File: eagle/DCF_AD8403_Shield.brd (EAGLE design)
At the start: 78.4 x 53.3 mm, 21 parts, among them IC1 TL072P, IC2 AD8403-100, J1 DCIN

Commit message: 基板図仮配線
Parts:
- removed JACK1, JACK2: MJ-353W-0, mylib2:MJ-3052W-0
- removed JP5: TS_SELECT, pinhead:1X03
- added U$1, U$2: AK_RCA_JACK_DIP, mylib2:AK_RCA_JACK_DIP
- moved R3 215.4 mm to (31.8, 33.0), turned to 180 degrees
- moved JP6 206.4 mm to (74.9, 27.9)
- moved C6 190.6 mm to (63.5, 43.2), turned to 90 degrees
- moved C7 187.5 mm to (63.5, 30.5), turned to 90 degrees
- moved C5 178.3 mm to (49.5, 43.2), turned to 180 degrees
- moved R1 161.3 mm to (53.3, 36.8), turned to 90 degrees
- moved R2 161.1 mm to (54.6, 30.5), turned to 180 degrees
- moved C4 160.6 mm to (44.5, 30.5), turned to 180 degrees
- moved C3 141.7 mm to (36.8, 27.9)
- moved C2 129.1 mm to (36.8, 35.6), turned to 180 degrees
- moved C1 128.1 mm to (36.8, 40.6), turned to 180 degrees
- moved J1 10.2 mm to (71.1, 38.1)
- moved IC2 7.62 mm to (29.2, 17.8)
- moved IC1 1.80 mm to (47.0, 36.8), turned to 270 degrees
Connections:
- removed net N$2: JACK1.2, JP5.1
- removed net N$4: JACK1.3, JP5.3
- net AGND: now also U$1.1, U$1.2, U$2.1, U$2.2; no longer JACK1.1, JACK2.1
- net BYPASS: now also U$1.3, U$1.4; no longer JACK2.3
- net FILTERED: now also U$2.3, U$2.4; no longer JACK2.2
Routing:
- net AGND: track 0.00 -> 148.0 mm
- net N$6: track 0.00 -> 87.6 mm
- net VSS: track 0.00 -> 61.1 mm
- net FILTERED: track 0.00 -> 60.1 mm
- net +5V: track 0.00 -> 48.3 mm
- net N$8: track 0.00 -> 47.1 mm
- net VDD: track 0.00 -> 43.6 mm
- net BYPASS: track 0.00 -> 38.7 mm
- net N$1: track 0.00 -> 32.6 mm
- net SCK: track 0.00 -> 25.7 mm
- net GND: track 0.00 -> 23.9 mm
- net N$5: track 0.00 -> 22.9 mm
- net MOSI: track 0.00 -> 10.2 mm
- net CS: track 0.00 -> 5.08 mm

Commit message: Update Eagle Files
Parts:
- removed U$1, U$2: AK_RCA_JACK_DIP, mylib2:AK_RCA_JACK_DIP
- added JK1: AK_RCA_JACK_DIP_REVERSE, mylib2:AK_RCA_JACK_DIP
- added JK2: AK_RCA_JACK_DIP, mylib2:AK_RCA_JACK_DIP
- added LED1: (no value), led:LED3MM
- added R4: 1k, rcl:0204/7
- C4, C5: value (none) -> 0.1uF
- C6, C7: value (none) -> 100uF; device rcl:SANYO-OSCON_E9 -> rcl:E2,5-6
- R1, R2: value (none) -> 100k
- R3: value (none) -> 0
- moved C1 25.4 mm to (36.8, 15.2)
- moved C2 22.7 mm to (26.7, 15.2), turned to 0 degrees
- moved C5 20.9 mm to (69.8, 38.1), turned to 0 degrees
- moved R1 18.5 mm to (71.1, 31.8)
- moved C4 18.5 mm to (62.2, 25.4)
- moved IC1 18.5 mm to (64.8, 31.8)
- moved R2 16.1 mm to (69.8, 25.4), turned to 0 degrees
- moved C7 13.3 mm to (76.2, 26.7), turned to 270 degrees
- moved IC2 11.4 mm to (34.3, 27.9)
- moved C3 10.5 mm to (39.4, 38.1), turned to 180 degrees
- moved R3 9.16 mm to (36.8, 25.4), turned to 0 degrees
- moved JP6 8.98 mm to (76.2, 36.8), turned to 90 degrees
- moved J1 7.62 mm to (71.1, 45.7)
- moved C6 1.27 mm to (62.2, 43.2), turned to 180 degrees
- turned JP1 to 180 degrees
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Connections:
- removed net VDD: C5.1, C6.+, IC1.8, J1.1, JP6.1, R1.2
- removed net VSS: C4.2, C7.-, IC1.4, J1.3, JP6.2, R2.1
- new net N$2: LED1.A, R4.1
- new net V+: C5.1, C6.+, IC1.8, J1.1, JP6.1, R1.2, R4.2
- new net V-: C4.2, C7.-, IC1.4, J1.3, JP6.2, LED1.K, R2.1
- net +5V: now also C3.1; no longer C3.2
- net AGND: now also C3.2, JK1.3, JK1.4, JK2.1, JK2.2, R3.1; no longer R3.2, U$1.1, U$1.2, U$2.1, U$2.2
- net BYPASS: now also JK1.1, JK1.2; no longer U$1.3, U$1.4
- net FILTERED: now also JK2.3, JK2.4; no longer U$2.3, U$2.4
- net GND: now also R3.2; no longer C3.1, R3.1
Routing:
- net N$6: track 87.6 -> 20.3 mm
- net V-: track 0.00 -> 65.1 mm
- net VSS: track 61.1 -> 0.00 mm
- net VDD: track 43.6 -> 0.00 mm
- net FILTERED: track 60.1 -> 85.1 mm
- net V+: track 0.00 -> 23.1 mm
- net N$1: track 32.6 -> 50.4 mm
- net CS: track 5.08 -> 22.0 mm
- net MOSI: track 10.2 -> 22.0 mm
- net SCK: track 25.7 -> 36.8 mm
- net N$8: track 47.1 -> 57.5 mm
- net AGND: track 148.0 -> 138.4 mm
- net GND: track 23.9 -> 33.2 mm
- net +5V: track 48.3 -> 39.2 mm
- net BYPASS: track 38.7 -> 32.6 mm
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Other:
- board size 78.4 x 53.3 mm -> 81 x 53.3 mm

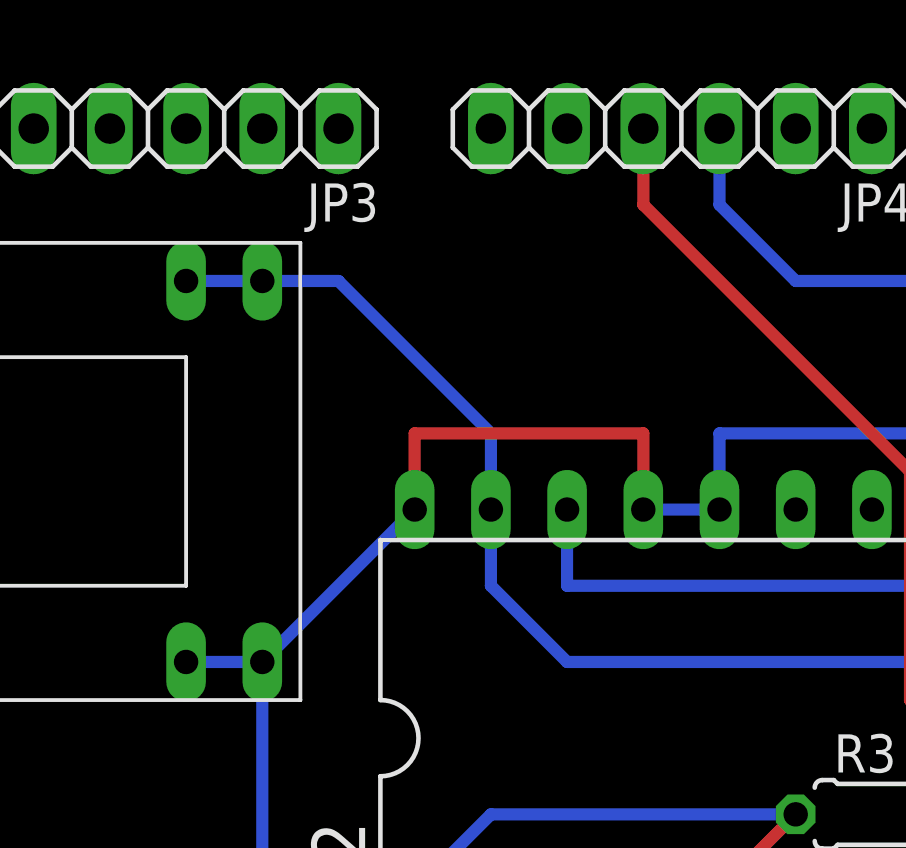
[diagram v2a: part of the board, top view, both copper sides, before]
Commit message: Add: output AC Coupling
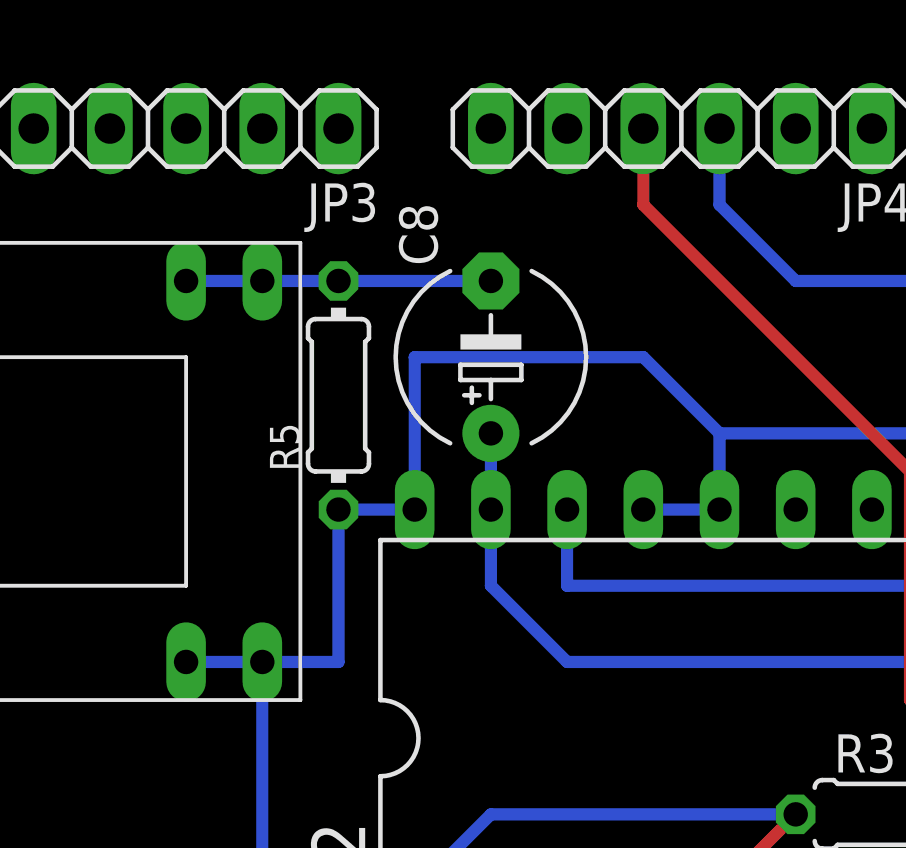
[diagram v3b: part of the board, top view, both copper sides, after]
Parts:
- added C8: 10uF, rcl:E5-6
- added R5: 10k, rcl:0204/7
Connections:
- new net N$3: C8.-, JK2.3, JK2.4, R5.2
- net AGND: now also R5.1
- net FILTERED: now also C8.+; no longer JK2.3, JK2.4
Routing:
- net FILTERED: track 85.1 -> 72.8 mm
- net N$3: track 0.00 -> 10.2 mm
- net AGND: track 138.4 -> 145.0 mm
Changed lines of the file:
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@@
 <element name="LED1" library="led" package="LED3MM" value="" x="60.96" y="49.53" rot="R270"/>
 <element name="R4" library="rcl" package="0204/7" value="1k" x="66.04" y="46.99" rot="R270"/>
+<element name="C8" library="rcl" package="E5-6" value="10uF" x="22.86" y="40.64" rot="R90"/>
+<element name="R5" library="rcl" package="0204/7" value="10k" x="17.78" y="39.37" rot="R90"/>
 </elements>
 <signals>
@@
 <contactref element="IC1" pad="1"/>
 <contactref element="IC2" pad="23"/>
-<contactref element="JK2" pad="3"/>
-<contactref element="JK2" pad="4"/>
-<wire x1="15.24" y1="43.18" x2="12.7" y2="43.18" width="0.4064" layer="16"/>
-<wire x1="15.24" y1="43.18" x2="17.78" y2="43.18" width="0.4064" layer="16"/>
-<wire x1="17.78" y1="43.18" x2="22.86" y2="38.1" width="0.4064" layer="16"/>
-<wire x1="22.86" y1="38.1" x2="22.86" y2="35.56" width="0.4064" layer="16"/>
 <wire x1="22.86" y1="35.56" x2="22.86" y2="33.02" width="0.4064" layer="16"/>
 <wire x1="22.86" y1="33.02" x2="25.4" y2="30.48" width="0.4064" layer="16"/>
@@
 <wire x1="53.34" y1="30.48" x2="58.42" y2="35.56" width="0.4064" layer="16"/>
 <wire x1="58.42" y1="35.56" x2="60.96" y2="35.56" width="0.4064" layer="16"/>
+<contactref element="C8" pad="+"/>
+<wire x1="22.86" y1="38.1" x2="22.86" y2="35.56" width="0.4064" layer="16"/>
 </signal>
 <signal name="N$1">
@@
 <wire x1="12.7" y1="22.86" x2="15.24" y2="22.86" width="0.4064" layer="16"/>
 <wire x1="15.24" y1="30.48" x2="15.24" y2="22.86" width="0.4064" layer="16"/>
-<wire x1="15.24" y1="30.48" x2="20.32" y2="35.56" width="0.4064" layer="16"/>
 <wire x1="15.24" y1="22.86" x2="17.78" y2="20.32" width="0.4064" layer="16"/>
 <wire x1="17.78" y1="20.32" x2="20.32" y2="20.32" width="0.4064" layer="16"/>
@@
 <wire x1="22.86" y1="25.4" x2="33.02" y2="25.4" width="0.4064" layer="16"/>
 <wire x1="27.94" y1="35.56" x2="30.48" y2="35.56" width="0.4064" layer="16"/>
-<wire x1="20.32" y1="35.56" x2="20.32" y2="38.1" width="0.4064" layer="1"/>
-<wire x1="20.32" y1="38.1" x2="27.94" y2="38.1" width="0.4064" layer="1"/>
-<wire x1="27.94" y1="38.1" x2="27.94" y2="35.56" width="0.4064" layer="1"/>
 <wire x1="68.58" y1="33.02" x2="68.58" y2="30.48" width="0.4064" layer="16"/>
 <wire x1="68.58" y1="33.02" x2="66.04" y2="33.02" width="0.4064" layer="16"/>
@@
 <wire x1="38.1" y1="40.64" x2="58.42" y2="40.64" width="0.4064" layer="1"/>
 <wire x1="58.42" y1="40.64" x2="60.96" y2="43.18" width="0.4064" layer="1"/>
+<contactref element="R5" pad="1"/>
+<wire x1="20.32" y1="35.56" x2="20.32" y2="40.64" width="0.4064" layer="16"/>
+<wire x1="20.32" y1="40.64" x2="27.94" y2="40.64" width="0.4064" layer="16"/>
+<wire x1="27.94" y1="40.64" x2="30.48" y2="38.1" width="0.4064" layer="16"/>
+<wire x1="17.78" y1="35.56" x2="20.32" y2="35.56" width="0.4064" layer="16"/>
+<wire x1="17.78" y1="35.56" x2="17.78" y2="30.48" width="0.4064" layer="16"/>
+<wire x1="17.78" y1="30.48" x2="15.24" y2="30.48" width="0.4064" layer="16"/>
+</signal>
+<signal name="N$3">
+<contactref element="C8" pad="-"/>
+<contactref element="JK2" pad="3"/>
+<contactref element="JK2" pad="4"/>
+<contactref element="R5" pad="2"/>
+<wire x1="12.7" y1="43.18" x2="15.24" y2="43.18" width="0.4064" layer="16"/>
+<wire x1="15.24" y1="43.18" x2="17.78" y2="43.18" width="0.4064" layer="16"/>
+<wire x1="17.78" y1="43.18" x2="22.86" y2="43.18" width="0.4064" layer="16"/>
 </signal>
 </signals>
